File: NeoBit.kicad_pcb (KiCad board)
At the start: 2 copper layers, 77.5 x 45.7 mm, 22 parts, among them J1 AudioJack3_Ground, J2 Barrel_Jack_MountingPin, J3 Qwiic, J4 DotStars, J5 microbit_edge_connector, J6 NeoPixels, U1 74AHCT125, U2 MCP1702-3302E_TO92, U3 MCP1702-5002E_TO92

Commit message: Get +V zone on correct net.
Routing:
- added copper zone on F.Cu, net +VDC
- removed copper zone on F.Cu, net +5V
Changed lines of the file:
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@@
   (gr_arc (start 121.285 127) (end 121.285 129.54) (angle 90) (layer Edge.Cuts) (width 0.15))
   (gr_arc (start 121.285 86.36) (end 118.745 86.36) (angle 90) (layer Edge.Cuts) (width 0.15))
-  (zone (net 1) (net_name +5V) (layer F.Cu) (hatch edge 0.508)
+  (zone (net 9) (net_name +VDC) (layer F.Cu) (hatch edge 0.508)
     (priority 1)
     (connect_pads (clearance 0.3048))

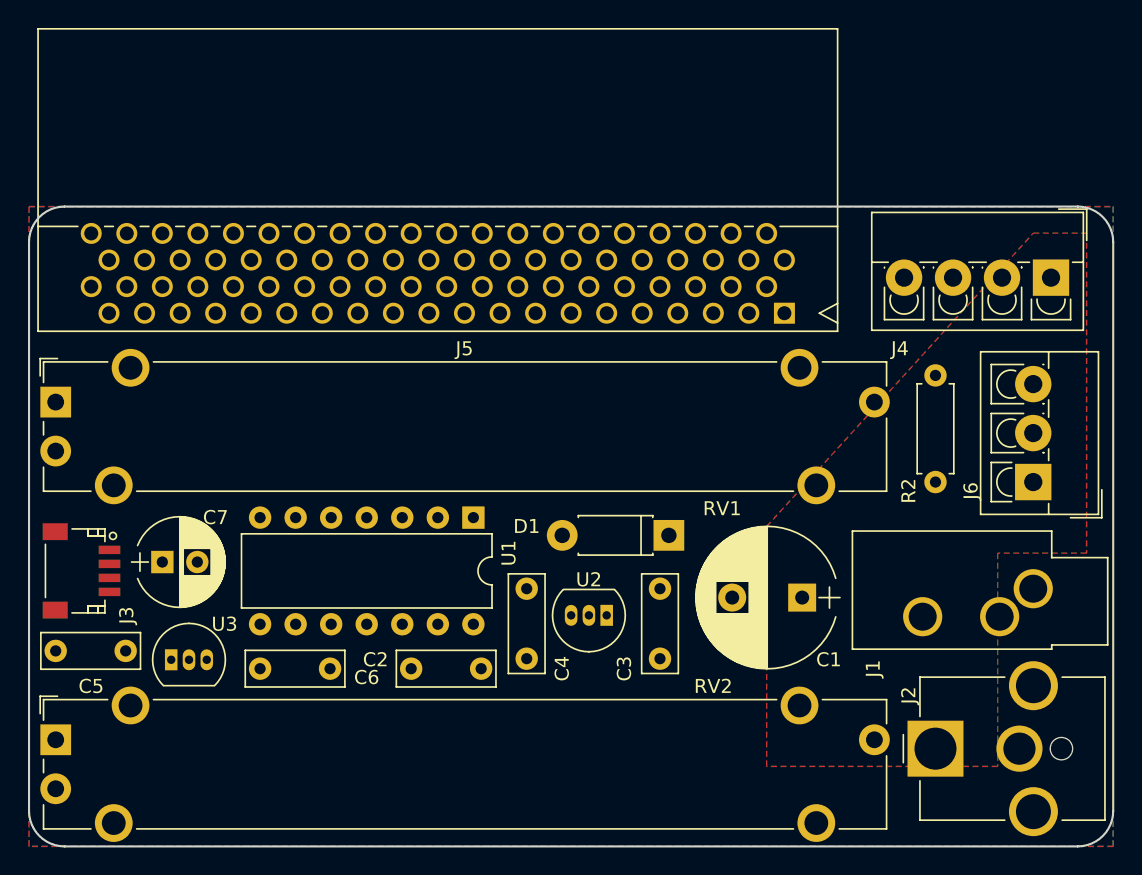
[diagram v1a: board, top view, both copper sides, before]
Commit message: Draw a few tracks.
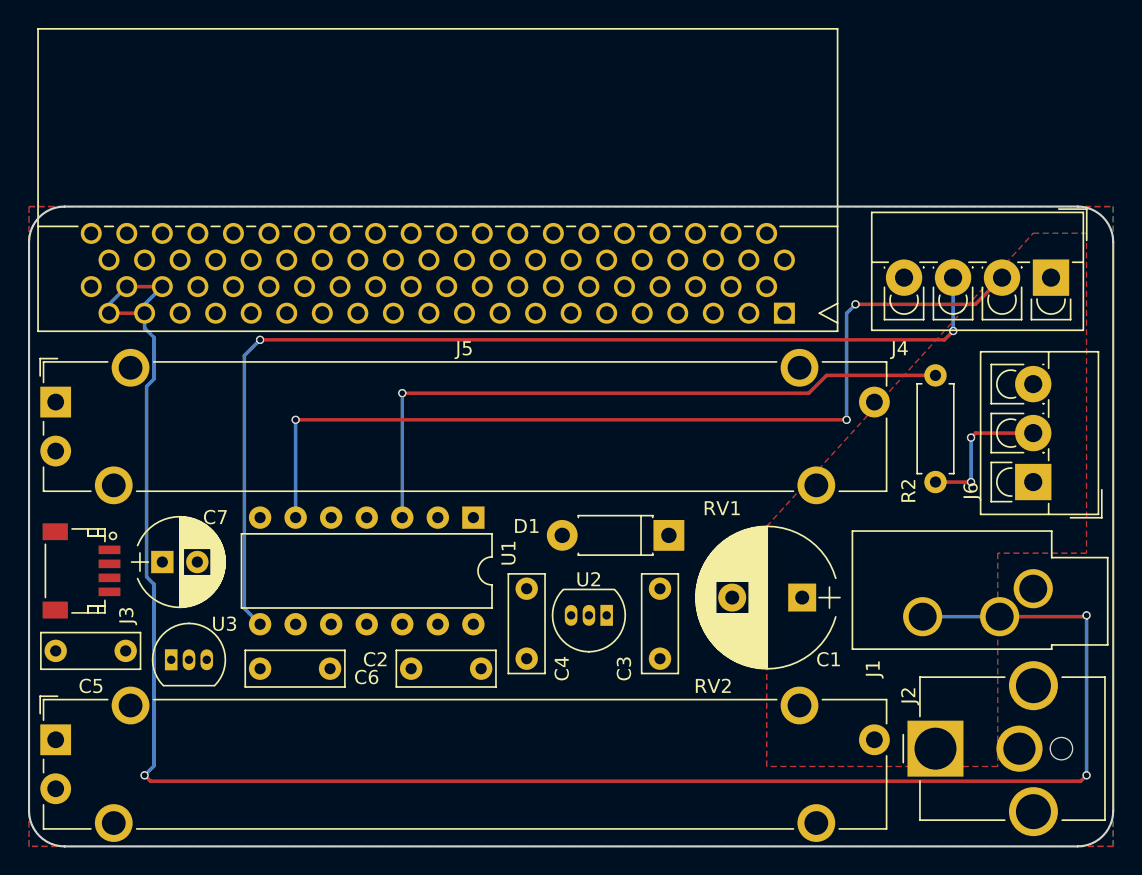
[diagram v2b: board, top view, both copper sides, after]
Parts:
- moved R2 7.62 mm to (183.5, 95.9), turned to 270 degrees
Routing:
- net /P0: track 0.00 -> 134.8 mm, vias 0 -> 3
- net /MOSI5: track 0.00 -> 74.9 mm, vias 0 -> 2
- net /SCK5: track 0.00 -> 66.1 mm, vias 0 -> 3
- net Net-(R2-Pad1): track 0.00 -> 47.5 mm, vias 0 -> 1
- net Net-(J6-Pad2): track 0.00 -> 10.3 mm, vias 0 -> 2
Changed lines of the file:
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@@
     (thickness 1.6)
     (drawings 14)
-    (tracks 0)
+    (tracks 54)
     (zones 0)
     (modules 22)
@@
     (pad_to_mask_clearance 0)
     (aux_axis_origin 0 0)
-    (visible_elements FFFEF77F)
+    (visible_elements FFFEE77F)
     (pcbplotparams
       (layerselection 0x010f0_80000001)
@@
   )
   (module Resistors_THT:R_Axial_DIN0207_L6.3mm_D2.5mm_P7.62mm_Horizontal (layer F.Cu)
-    (at 183.515 103.505 90)
+    (at 183.515 95.885 270)
     (descr "Resistor, Axial_DIN0207 series, Axial, Horizontal, pin pitch=7.62mm, 0.25W = 1/4W, length*diameter=6.3*2.5mm^2, http://cdn-reichelt.de/documents/datenblatt/B400/1_4W%23YAG.pdf")
     (tags "Resistor Axial_DIN0207 series Axial Horizontal pin pitch 7.62mm 0.25W = 1/4W length 6.3mm diameter 2.5mm")
-    (fp_text reference R2 (at -0.635 -1.905 90) (layer F.SilkS)
-      (effects (font (size 1 1) (thickness 0.15)))
-    )
-    (fp_text value 470 (at 3.81 2.31 90) (layer F.Fab)
+    (fp_text reference R2 (at 8.255 1.905 270) (layer F.SilkS)
+      (effects (font (size 1 1) (thickness 0.15)))
+    )
+    (fp_text value 470 (at 3.81 2.31 270) (layer F.Fab)
       (effects (font (size 1 1) (thickness 0.15)))
     )
@@
     (fp_line (start 8.7 1.6) (end 8.7 -1.6) (layer F.CrtYd) (width 0.05))
     (fp_line (start 8.7 -1.6) (end -1.05 -1.6) (layer F.CrtYd) (width 0.05))
-    (pad 1 thru_hole circle (at 0 0 90) (size 1.6 1.6) (drill 0.8) (layers *.Cu *.Mask)
+    (pad 1 thru_hole circle (at 0 0 270) (size 1.6 1.6) (drill 0.8) (layers *.Cu *.Mask)
       (net 8 "Net-(R2-Pad1)"))
-    (pad 2 thru_hole oval (at 7.62 0 90) (size 1.6 1.6) (drill 0.8) (layers *.Cu *.Mask)
+    (pad 2 thru_hole oval (at 7.62 0 270) (size 1.6 1.6) (drill 0.8) (layers *.Cu *.Mask)
       (net 15 "Net-(J6-Pad2)"))
     (model ${KISYS3DMOD}/Resistors_THT.3dshapes/R_Axial_DIN0207_L6.3mm_D2.5mm_P7.62mm_Horizontal.wrl
@@
   (gr_arc (start 121.285 127) (end 121.285 129.54) (angle 90) (layer Edge.Cuts) (width 0.15))
   (gr_arc (start 121.285 86.36) (end 118.745 86.36) (angle 90) (layer Edge.Cuts) (width 0.15))
+  (segment (start 124.46 91.44) (end 127 91.44) (width 0.25) (layer F.Cu) (net 5))
+  (segment (start 125.73 89.54) (end 128.27 89.54) (width 0.25) (layer F.Cu) (net 5))
+  (segment (start 124.46 91.44) (end 124.46 90.81) (width 0.25) (layer B.Cu) (net 5))
+  (segment (start 124.46 90.81) (end 125.73 89.54) (width 0.25) (layer B.Cu) (net 5))
+  (segment (start 127 91.44) (end 127 90.81) (width 0.25) (layer B.Cu) (net 5))
+  (segment (start 127 90.81) (end 128.27 89.54) (width 0.25) (layer B.Cu) (net 5))
+  (segment (start 127 124.46) (end 127.675001 123.784999) (width 0.25) (layer B.Cu) (net 5))
+  (segment (start 127.675001 123.784999) (end 127.675001 110.810003) (width 0.25) (layer B.Cu) (net 5))
+  (segment (start 127.675001 110.810003) (end 127.144999 110.280001) (width 0.25) (layer B.Cu) (net 5))
+  (segment (start 127.144999 110.280001) (end 127.144999 96.674003) (width 0.25) (layer B.Cu) (net 5))
+  (segment (start 127.144999 96.674003) (end 127.675001 96.144001) (width 0.25) (layer B.Cu) (net 5))
+  (segment (start 127.675001 96.144001) (end 127.675001 93.175661) (width 0.25) (layer B.Cu) (net 5))
+  (segment (start 127.675001 93.175661) (end 127 92.50066) (width 0.25) (layer B.Cu) (net 5))
+  (segment (start 127 92.50066) (end 127 91.44) (width 0.25) (layer B.Cu) (net 5))
+  (segment (start 194.31 124.46) (end 193.889999 124.880001) (width 0.25) (layer F.Cu) (net 5))
+  (segment (start 193.889999 124.880001) (end 127.420001 124.880001) (width 0.25) (layer F.Cu) (net 5))
+  (segment (start 127.420001 124.880001) (end 127 124.46) (width 0.25) (layer F.Cu) (net 5))
+  (via (at 127 124.46) (size 0.6) (drill 0.4) (layers F.Cu B.Cu) (net 5))
+  (segment (start 194.31 113.03) (end 194.31 124.46) (width 0.25) (layer B.Cu) (net 5))
+  (via (at 194.31 124.46) (size 0.6) (drill 0.4) (layers F.Cu B.Cu) (net 5))
+  (segment (start 188.1 113.125) (end 194.215 113.125) (width 0.25) (layer F.Cu) (net 5))
+  (segment (start 194.215 113.125) (end 194.31 113.03) (width 0.25) (layer F.Cu) (net 5))
+  (via (at 194.31 113.03) (size 0.6) (drill 0.4) (layers F.Cu B.Cu) (net 5))
+  (segment (start 182.6 113.125) (end 188.1 113.125) (width 0.25) (layer B.Cu) (net 5))
+  (segment (start 145.415 97.155) (end 145.415 106.045) (width 0.25) (layer B.Cu) (net 8))
+  (segment (start 183.515 95.885) (end 175.734002 95.885) (width 0.25) (layer F.Cu) (net 8))
+  (segment (start 175.734002 95.885) (end 174.464002 97.155) (width 0.25) (layer F.Cu) (net 8))
+  (segment (start 174.464002 97.155) (end 145.415 97.155) (width 0.25) (layer F.Cu) (net 8))
+  (via (at 145.415 97.155) (size 0.6) (drill 0.4) (layers F.Cu B.Cu) (net 8))
+  (segment (start 186.055 103.505) (end 183.515 103.505) (width 0.25) (layer F.Cu) (net 15))
+  (segment (start 186.055 100.33) (end 186.055 103.505) (width 0.25) (layer B.Cu) (net 15))
+  (via (at 186.055 103.505) (size 0.6) (drill 0.4) (layers F.Cu B.Cu) (net 15))
+  (segment (start 190.5 100.005) (end 186.38 100.005) (width 0.25) (layer F.Cu) (net 15))
+  (segment (start 186.38 100.005) (end 186.055 100.33) (width 0.25) (layer F.Cu) (net 15))
+  (via (at 186.055 100.33) (size 0.6) (drill 0.4) (layers F.Cu B.Cu) (net 15))
+  (segment (start 137.795 99.06) (end 137.795 106.045) (width 0.25) (layer B.Cu) (net 16))
+  (segment (start 177.165 99.06) (end 137.795 99.06) (width 0.25) (layer F.Cu) (net 16))
+  (via (at 137.795 99.06) (size 0.6) (drill 0.4) (layers F.Cu B.Cu) (net 16))
+  (segment (start 177.8 90.805) (end 177.165 91.44) (width 0.25) (layer B.Cu) (net 16))
+  (segment (start 177.165 91.44) (end 177.165 99.06) (width 0.25) (layer B.Cu) (net 16))
+  (via (at 177.165 99.06) (size 0.6) (drill 0.4) (layers F.Cu B.Cu) (net 16))
+  (segment (start 188.27 88.9) (end 186.365 90.805) (width 0.25) (layer F.Cu) (net 16))
+  (segment (start 186.365 90.805) (end 177.8 90.805) (width 0.25) (layer F.Cu) (net 16))
+  (via (at 177.8 90.805) (size 0.6) (drill 0.4) (layers F.Cu B.Cu) (net 16))
+  (segment (start 135.255 93.345) (end 134.129999 94.470001) (width 0.25) (layer B.Cu) (net 17))
+  (segment (start 134.129999 94.470001) (end 134.129999 112.539999) (width 0.25) (layer B.Cu) (net 17))
+  (segment (start 134.129999 112.539999) (end 134.455001 112.865001) (width 0.25) (layer B.Cu) (net 17))
+  (segment (start 134.455001 112.865001) (end 135.255 113.665) (width 0.25) (layer B.Cu) (net 17))
+  (segment (start 184.785 92.71) (end 184.15 93.345) (width 0.25) (layer F.Cu) (net 17))
+  (segment (start 184.15 93.345) (end 135.255 93.345) (width 0.25) (layer F.Cu) (net 17))
+  (via (at 135.255 93.345) (size 0.6) (drill 0.4) (layers F.Cu B.Cu) (net 17))
+  (segment (start 184.77 88.9) (end 184.77 92.695) (width 0.25) (layer B.Cu) (net 17))
+  (segment (start 184.77 92.695) (end 184.785 92.71) (width 0.25) (layer B.Cu) (net 17))
+  (via (at 184.785 92.71) (size 0.6) (drill 0.4) (layers F.Cu B.Cu) (net 17))
   (zone (net 9) (net_name +VDC) (layer F.Cu) (hatch edge 0.508)
     (priority 1)

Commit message: Added some more tracks.
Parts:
- moved C5 14.7 mm to (135.3, 116.8)
- moved C6 9.61 mm to (125.7, 115.6), turned to 180 degrees
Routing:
- net +VDC: track 0.00 -> 61.8 mm
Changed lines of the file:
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@@
   (general
     (links 81)
-    (no_connects 57)
+    (no_connects 46)
     (area 118.669999 83.744999 186.130001 129.615001)
     (thickness 1.6)
     (drawings 14)
-    (tracks 54)
+    (tracks 67)
     (zones 0)
     (modules 22)
@@
   )
   (setup
-    (last_trace_width 0.25)
+    (last_trace_width 0.508)
     (user_trace_width 0.508)
     (user_trace_width 1.016)
@@
   )
   (module Capacitors_THT:C_Rect_L7.0mm_W2.5mm_P5.00mm (layer F.Cu)
-    (at 120.65 115.57)
+    (at 135.255 116.84)
     (descr "C, Rect series, Radial, pin pitch=5.00mm, , length*width=7*2.5mm^2, Capacitor")
     (tags "C Rect series Radial pin pitch 5.00mm  length 7mm width 2.5mm Capacitor")
-    (fp_text reference C5 (at 2.54 2.54) (layer F.SilkS)
+    (fp_text reference C5 (at 7.62 0.635) (layer F.SilkS)
       (effects (font (size 1 1) (thickness 0.15)))
     )
@@
   )
   (module Capacitors_THT:C_Rect_L7.0mm_W2.5mm_P5.00mm (layer F.Cu)
-    (at 135.255 116.84)
+    (at 125.73 115.57 180)
     (descr "C, Rect series, Radial, pin pitch=5.00mm, , length*width=7*2.5mm^2, Capacitor")
     (tags "C Rect series Radial pin pitch 5.00mm  length 7mm width 2.5mm Capacitor")
-    (fp_text reference C6 (at 7.62 0.635) (layer F.SilkS)
-      (effects (font (size 1 1) (thickness 0.15)))
-    )
-    (fp_text value 1µF (at 2.5 2.56) (layer F.Fab)
+    (fp_text reference C6 (at 2.54 -2.54 180) (layer F.SilkS)
+      (effects (font (size 1 1) (thickness 0.15)))
+    )
+    (fp_text value 1µF (at 2.5 2.56 180) (layer F.Fab)
       (effects (font (size 1 1) (thickness 0.15)))
     )
@@
     (fp_line (start 6.35 1.6) (end 6.35 -1.6) (layer F.CrtYd) (width 0.05))
     (fp_line (start 6.35 -1.6) (end -1.35 -1.6) (layer F.CrtYd) (width 0.05))
-    (fp_text user %R (at 2.5 0) (layer F.Fab)
-      (effects (font (size 1 1) (thickness 0.15)))
-    )
-    (pad 1 thru_hole circle (at 0 0) (size 1.6 1.6) (drill 0.8) (layers *.Cu *.Mask)
+    (fp_text user %R (at 2.5 0 180) (layer F.Fab)
+      (effects (font (size 1 1) (thickness 0.15)))
+    )
+    (pad 1 thru_hole circle (at 0 0 180) (size 1.6 1.6) (drill 0.8) (layers *.Cu *.Mask)
       (net 1 +5V))
-    (pad 2 thru_hole circle (at 5 0) (size 1.6 1.6) (drill 0.8) (layers *.Cu *.Mask)
+    (pad 2 thru_hole circle (at 5 0 180) (size 1.6 1.6) (drill 0.8) (layers *.Cu *.Mask)
       (net 2 GND))
     (model ${KISYS3DMOD}/Capacitors_THT.3dshapes/C_Rect_L7.0mm_W2.5mm_P5.00mm.wrl
@@
   (segment (start 174.464002 97.155) (end 145.415 97.155) (width 0.25) (layer F.Cu) (net 8))
   (via (at 145.415 97.155) (size 0.6) (drill 0.4) (layers F.Cu B.Cu) (net 8))
+  (segment (start 173.99 115.57) (end 171.465999 118.094001) (width 0.508) (layer F.Cu) (net 9))
+  (segment (start 171.465999 118.094001) (end 136.509001 118.094001) (width 0.508) (layer F.Cu) (net 9))
+  (segment (start 136.509001 118.094001) (end 136.054999 117.639999) (width 0.508) (layer F.Cu) (net 9))
+  (segment (start 136.054999 117.639999) (end 135.255 116.84) (width 0.508) (layer F.Cu) (net 9))
+  (segment (start 173.99 111.76) (end 173.99 115.57) (width 0.508) (layer F.Cu) (net 9))
+  (segment (start 163.83 111.125) (end 159.397 111.125) (width 0.508) (layer F.Cu) (net 9))
+  (segment (start 159.397 111.125) (end 158.75 111.772) (width 0.508) (layer F.Cu) (net 9))
+  (segment (start 158.75 111.772) (end 158.75 113.03) (width 0.508) (layer F.Cu) (net 9))
+  (segment (start 173.99 111.76) (end 172.482 111.76) (width 0.508) (layer F.Cu) (net 9))
+  (segment (start 172.482 111.76) (end 171.027999 110.305999) (width 0.508) (layer F.Cu) (net 9))
+  (segment (start 171.027999 110.305999) (end 164.649001 110.305999) (width 0.508) (layer F.Cu) (net 9))
+  (segment (start 164.649001 110.305999) (end 164.629999 110.325001) (width 0.508) (layer F.Cu) (net 9))
+  (segment (start 164.629999 110.325001) (end 163.83 111.125) (width 0.508) (layer F.Cu) (net 9))
   (segment (start 186.055 103.505) (end 183.515 103.505) (width 0.25) (layer F.Cu) (net 15))
   (segment (start 186.055 100.33) (end 186.055 103.505) (width 0.25) (layer B.Cu) (net 15))

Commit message: More tracks.
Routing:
- net +5V: track 0.00 -> 28.5 mm
- net +3V3: track 0.00 -> 24.2 mm, vias 0 -> 1
- net Net-(C4-Pad1): track 0.00 -> 8.83 mm
- net +VDC: track 61.8 -> 67.8 mm
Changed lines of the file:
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@@
     (thickness 1.6)
     (drawings 14)
-    (tracks 67)
+    (tracks 90)
     (zones 0)
     (modules 22)
@@
   (gr_arc (start 121.285 127) (end 121.285 129.54) (angle 90) (layer Edge.Cuts) (width 0.15))
   (gr_arc (start 121.285 86.36) (end 118.745 86.36) (angle 90) (layer Edge.Cuts) (width 0.15))
+  (segment (start 146.05 116.84) (end 147.32 116.84) (width 0.508) (layer F.Cu) (net 1))
+  (segment (start 147.32 116.84) (end 150.495 113.665) (width 0.508) (layer F.Cu) (net 1))
+  (segment (start 131.445 116.205) (end 132.403 116.205) (width 0.508) (layer F.Cu) (net 1))
+  (segment (start 132.403 116.205) (end 133.022001 115.585999) (width 0.508) (layer F.Cu) (net 1))
+  (segment (start 133.022001 115.585999) (end 144.795999 115.585999) (width 0.508) (layer F.Cu) (net 1))
+  (segment (start 144.795999 115.585999) (end 145.250001 116.040001) (width 0.508) (layer F.Cu) (net 1))
+  (segment (start 145.250001 116.040001) (end 146.05 116.84) (width 0.508) (layer F.Cu) (net 1))
+  (segment (start 125.73 115.57) (end 126.529999 114.770001) (width 0.508) (layer F.Cu) (net 1))
+  (segment (start 126.529999 114.770001) (end 131.268001 114.770001) (width 0.508) (layer F.Cu) (net 1))
+  (segment (start 131.268001 114.770001) (end 131.445 114.947) (width 0.508) (layer F.Cu) (net 1))
+  (segment (start 131.445 114.947) (end 131.445 116.205) (width 0.508) (layer F.Cu) (net 1))
+  (segment (start 154.305 111.125) (end 154.305 109.855) (width 0.508) (layer B.Cu) (net 3))
+  (segment (start 154.305 109.855) (end 156.845 107.315) (width 0.508) (layer B.Cu) (net 3))
+  (segment (start 157.48 113.03) (end 156.21 113.03) (width 0.508) (layer F.Cu) (net 3))
+  (segment (start 156.21 113.03) (end 154.305 111.125) (width 0.508) (layer F.Cu) (net 3))
+  (segment (start 164.465 97.79) (end 179.15 97.79) (width 0.508) (layer F.Cu) (net 4))
+  (segment (start 164.465 107.315) (end 164.465 97.79) (width 0.508) (layer B.Cu) (net 4))
+  (via (at 164.465 97.79) (size 0.6) (drill 0.4) (layers F.Cu B.Cu) (net 4))
   (segment (start 124.46 91.44) (end 127 91.44) (width 0.25) (layer F.Cu) (net 5))
   (segment (start 125.73 89.54) (end 128.27 89.54) (width 0.25) (layer F.Cu) (net 5))
@@
   (segment (start 174.464002 97.155) (end 145.415 97.155) (width 0.25) (layer F.Cu) (net 8))
   (via (at 145.415 97.155) (size 0.6) (drill 0.4) (layers F.Cu B.Cu) (net 8))
+  (segment (start 135.255 116.84) (end 134.12363 116.84) (width 0.508) (layer F.Cu) (net 9))
+  (segment (start 134.12363 116.84) (end 133.55462 117.40901) (width 0.508) (layer F.Cu) (net 9))
+  (segment (start 131.070547 117.40901) (end 130.175 116.513463) (width 0.508) (layer F.Cu) (net 9))
+  (segment (start 133.55462 117.40901) (end 131.070547 117.40901) (width 0.508) (layer F.Cu) (net 9))
+  (segment (start 130.175 116.513463) (end 130.175 116.205) (width 0.508) (layer F.Cu) (net 9))
   (segment (start 173.99 115.57) (end 171.465999 118.094001) (width 0.508) (layer F.Cu) (net 9))
   (segment (start 171.465999 118.094001) (end 136.509001 118.094001) (width 0.508) (layer F.Cu) (net 9))

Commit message: Finished wiring power tracks.
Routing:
- net +3V3: track 24.2 -> 119.3 mm, vias 1 -> 2
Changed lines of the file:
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@@
     (thickness 1.6)
     (drawings 14)
-    (tracks 90)
+    (tracks 115)
     (zones 0)
     (modules 22)
@@
   (segment (start 157.48 113.03) (end 156.21 113.03) (width 0.508) (layer F.Cu) (net 3))
   (segment (start 156.21 113.03) (end 154.305 111.125) (width 0.508) (layer F.Cu) (net 3))
+  (segment (start 165.1 121.92) (end 179.15 121.92) (width 0.508) (layer F.Cu) (net 4))
+  (segment (start 164.465 107.315) (end 164.465 109.904078) (width 0.508) (layer B.Cu) (net 4))
+  (via (at 165.1 121.92) (size 0.6) (drill 0.4) (layers F.Cu B.Cu) (net 4))
+  (segment (start 164.465 109.904078) (end 165.1 110.539078) (width 0.508) (layer B.Cu) (net 4))
+  (segment (start 165.1 110.539078) (end 165.1 121.92) (width 0.508) (layer B.Cu) (net 4))
+  (segment (start 128.27 109.22) (end 124.6275 109.22) (width 0.508) (layer F.Cu) (net 4))
+  (segment (start 124.6275 109.22) (end 124.4925 109.355) (width 0.508) (layer F.Cu) (net 4))
+  (segment (start 164.465 107.315) (end 159.144922 107.315) (width 0.508) (layer F.Cu) (net 4))
+  (segment (start 159.144922 107.315) (end 157.590921 108.869001) (width 0.508) (layer F.Cu) (net 4))
+  (segment (start 157.590921 108.869001) (end 132.274923 108.869001) (width 0.508) (layer F.Cu) (net 4))
+  (segment (start 132.274923 108.869001) (end 131.371921 107.965999) (width 0.508) (layer F.Cu) (net 4))
+  (segment (start 131.371921 107.965999) (end 129.524001 107.965999) (width 0.508) (layer F.Cu) (net 4))
+  (segment (start 129.524001 107.965999) (end 128.27 109.22) (width 0.508) (layer F.Cu) (net 4))
+  (segment (start 160.02 91.44) (end 162.56 91.44) (width 0.508) (layer F.Cu) (net 4))
+  (segment (start 157.48 91.44) (end 160.02 91.44) (width 0.508) (layer F.Cu) (net 4))
+  (segment (start 158.75 89.54) (end 161.29 89.54) (width 0.508) (layer F.Cu) (net 4))
+  (segment (start 156.21 89.54) (end 158.75 89.54) (width 0.508) (layer F.Cu) (net 4))
+  (segment (start 157.48 91.44) (end 157.48 90.81) (width 0.508) (layer B.Cu) (net 4))
+  (segment (start 157.48 90.81) (end 156.21 89.54) (width 0.508) (layer B.Cu) (net 4))
+  (segment (start 160.02 91.44) (end 160.02 90.81) (width 0.508) (layer B.Cu) (net 4))
+  (segment (start 160.02 90.81) (end 158.75 89.54) (width 0.508) (layer B.Cu) (net 4))
+  (segment (start 162.56 91.44) (end 162.56 90.81) (width 0.508) (layer B.Cu) (net 4))
+  (segment (start 162.56 90.81) (end 161.29 89.54) (width 0.508) (layer B.Cu) (net 4))
+  (segment (start 164.465 97.79) (end 164.465 93.345) (width 0.508) (layer B.Cu) (net 4))
+  (segment (start 164.465 93.345) (end 162.56 91.44) (width 0.508) (layer B.Cu) (net 4))
   (segment (start 164.465 97.79) (end 179.15 97.79) (width 0.508) (layer F.Cu) (net 4))
   (segment (start 164.465 107.315) (end 164.465 97.79) (width 0.508) (layer B.Cu) (net 4))

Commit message: I think I've routed all the tracks.
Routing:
- net /P2: track 0.00 -> 71.3 mm, vias 0 -> 1
- net /SCL: track 0.00 -> 63.1 mm, vias 0 -> 1
- net /SDA: track 0.00 -> 61.3 mm, vias 0 -> 1
- net /MOSI: track 0.00 -> 39.3 mm, vias 0 -> 2
- net /P1: track 0.00 -> 32.8 mm, vias 0 -> 1
- net /SCK: track 0.00 -> 27.3 mm, vias 0 -> 2
- net /P16: track 0.00 -> 21.6 mm, vias 0 -> 2
